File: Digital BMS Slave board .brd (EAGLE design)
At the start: 54.6 x 100 mm, 91 parts, among them J1 S7B-PH-K

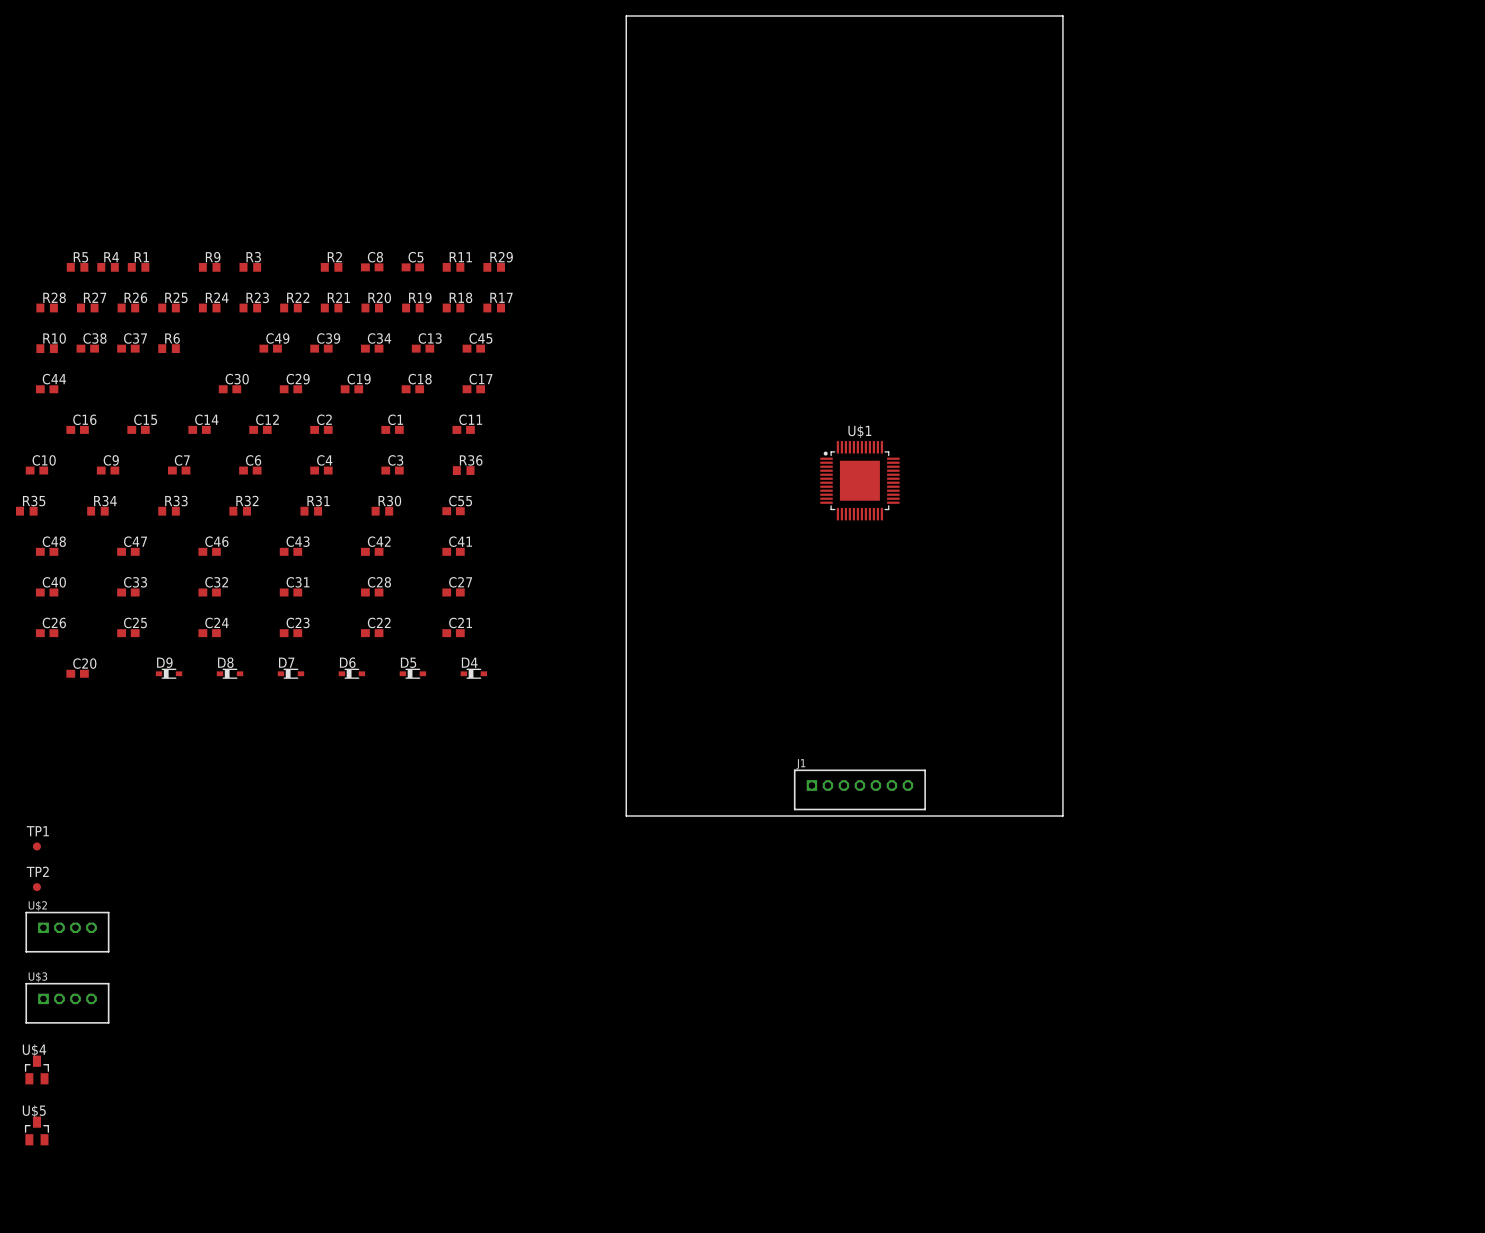
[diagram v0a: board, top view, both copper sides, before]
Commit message: Board size to chek
The schematic file is close to release ver.
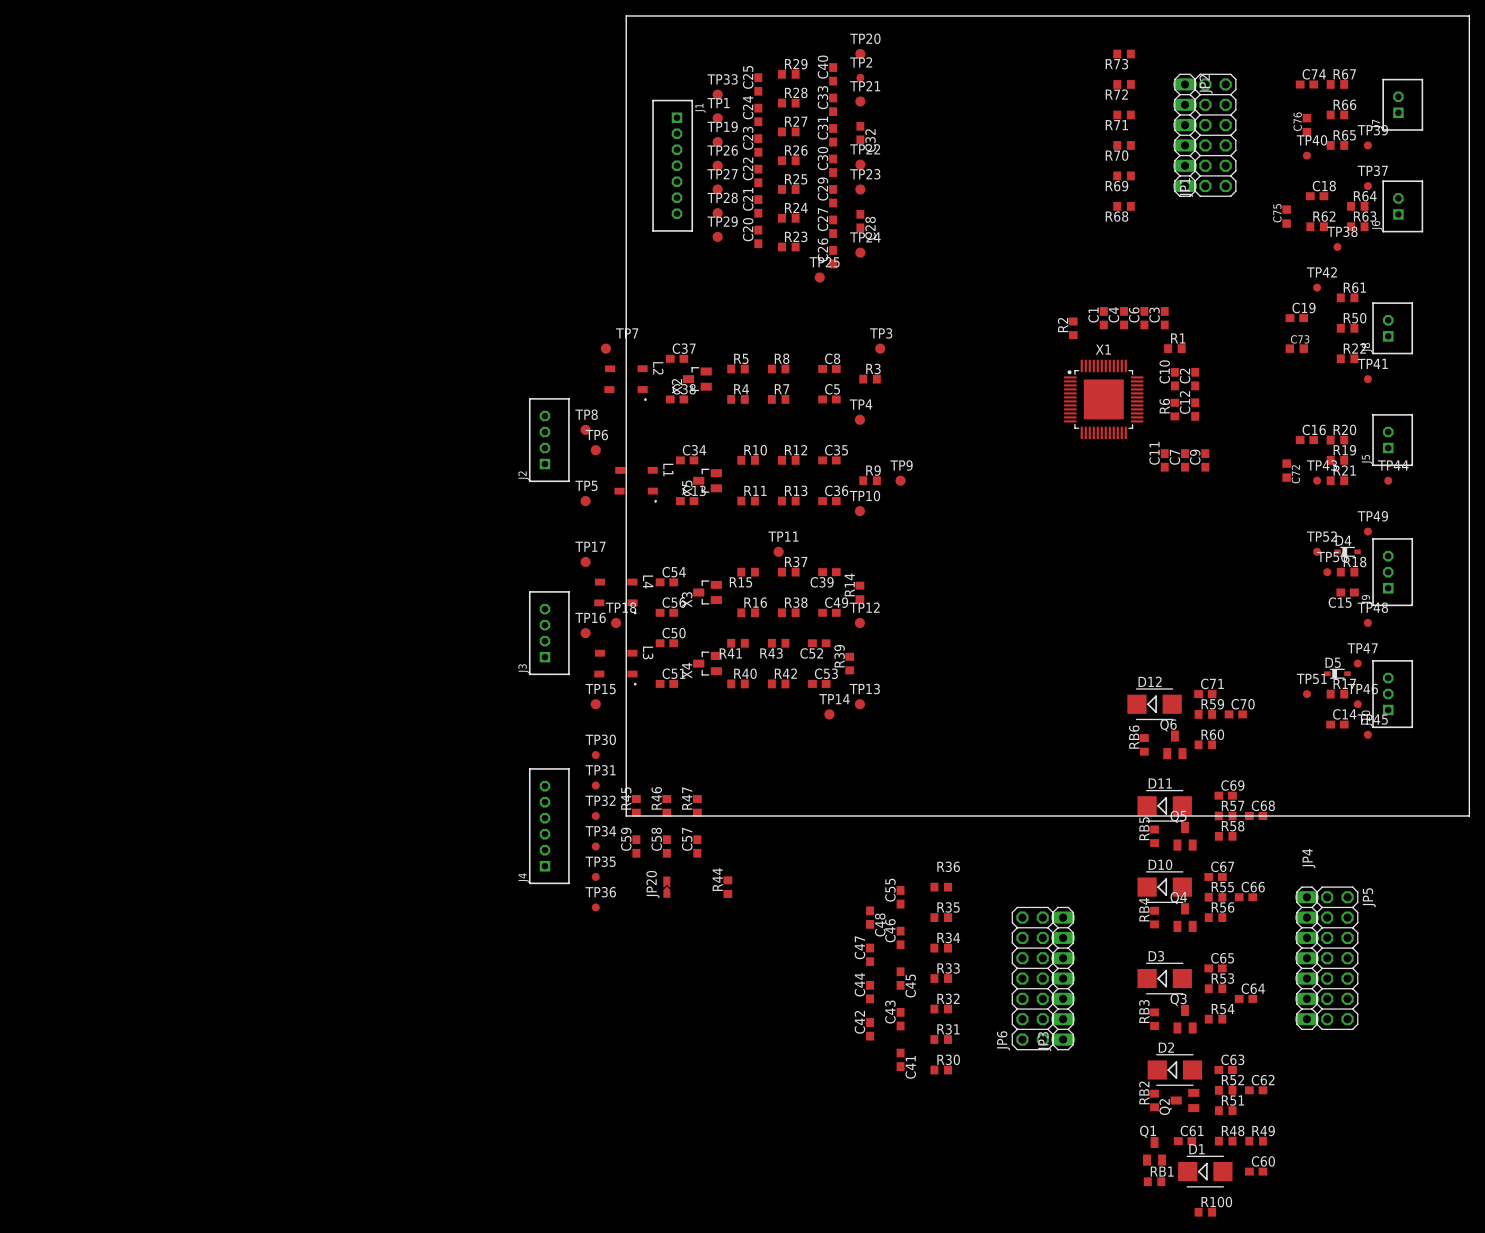
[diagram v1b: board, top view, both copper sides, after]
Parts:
- removed C17: 1u/16V, resistor:C0603
- removed D6, D7, D8, D9: BAT60J, diode:SOD323_ST
- removed U$1: BQ79606A-Q1-HTQFP(PHP)|48, texas Instrumets:QFP50P900X900X105-49T500
- removed U$2, U$3: S4B-PH-K, con-jst-ph:S4B-PH-K
- removed U$4, U$5: PESD2CAN, stmicroelectronics:SOT23
- added C35, C36, C52, C53, C57: 51p, resistor:C0603
- added C50, C51, C54, C56: 2200p, resistor:C0603
- added C58, C59: 1nF, resistor:C0603
- added C60, C61, C62, C63, C64, C65, C66, C67, C68, C69, C70, C71, C74: 1u/16V, resistor:C0603
- added C72, C73, C75, C76: 1u/16V, Capacitors:C0603K-X
- added D1, D10, D11, D12, D2, D3: (no value), eagle-ltspice:DIODE_SMB
- added J10, J9: S3B-PH-K, con-jst-ph:S3B-PH-K
- added J2, J3: S4B-PH-K, con-jst-ph:S4B-PH-K
- added J4: S6B-PH-K, con-jst-ph:S6B-PH-K
- added J5, J6, J7, J8: S2B-PH-K, con-jst-ph:S2B-PH-K
- added JP1: (no value), pinhead:2X06
- added JP2: (no value), pinhead:1X06
- added JP20: SOLDER_BRIDGE, testing:SOLDER_BRIDGE
- added JP3, JP4: (no value), pinhead:1X07
- added JP5, JP6: (no value), pinhead:2X07
- added L1, L2, L3, L4: 100uH, Inductors:ACT45B
- added Q1, Q2, Q3, Q4, Q5, Q6: BSS123, transistor-small-signal:SOT23
- added R100, R49, R52, R54, R56, R58, R60: 100, resistor:R0603
- added R12, R13, R37, R38, R42, R43, R7, R8: 43, resistor:R0603
- added R14, R39: 10k, resistor:R0603
- added R15, R16, R40, R41: 10, resistor:R0603
- added R44, R45, R46, R47: 100k, resistor:R0603
- added R48, R51, R53, R55, R57, R59, R62, R65: 1k, resistor:R0603
- added R50, R61, R63, R64, R66, R67: (no value), Resistors:R0603
- added R68, R69, R70, R71, R72, R73: 10k, Resistors:R0603
- added RB1, RB2, RB3, RB4, RB5, RB6: 20, resistor:R0603
- added TP10, TP11, TP12, TP13, TP14, TP15, TP16, TP17, TP18, TP19, TP20, TP21, TP22, TP23, TP24, TP25, TP26, TP27, TP28, TP29, TP3, TP33, TP4, TP5, TP6, TP7, TP8, TP9: TEST_PAD2, testing:TP1.27MM_MASK
- added TP30, TP31, TP32, TP34, TP35, TP36, TP37, TP38, TP39, TP40, TP41, TP42, TP43, TP44, TP45, TP46, TP47, TP48, TP49, TP50, TP51, TP52: TEST_PAD, testing:TP1MM_MASK
- added X1: BQ79606A-Q1-HTQFP(PHP)|48, texas Instrumets:QFP50P900X900X105-49T500
- added X2, X3, X4, X5: PESD2CAN, stmicroelectronics:SOT23
- C37, C38: value 51p -> 2200p
- C39, C49: value 2200p -> 51p
- D4, D5: value BAT60J -> 6.5V
- R10, R11, R4, R5: value 49 -> 10
- R20, R21: value 1k -> (none); device resistor:R0603 -> Resistors:R0603
- TP1: value TEST_PAD -> TEST_PAD2; device testing:TP1MM_MASK -> testing:TP1.27MM_MASK
- moved C16 153.7 mm to (85.1, 47.0)
- moved C15 152.5 mm to (90.2, 27.9), turned to 180 degrees
- moved C14 146.9 mm to (88.9, 11.4)
- moved TP2 144.3 mm to (29.3, 92.3)
- moved C10 142.7 mm to (68.6, 54.6), turned to 90 degrees
- moved C9 137.2 mm to (72.4, 44.5), turned to 90 degrees
- moved R22 132.2 mm to (90.2, 57.1)
- moved R1 129.9 mm to (68.6, 58.4)
- moved R21 127.6 mm to (88.9, 41.9)
- moved C44 127.5 mm to (30.5, -22.0), turned to 90 degrees
- moved R6 126.0 mm to (68.6, 50.8), turned to 90 degrees
- moved C7 125.7 mm to (69.8, 44.5), turned to 90 degrees
- moved R35 125.1 mm to (39.4, -12.7)
- moved TP1 124.6 mm to (11.4, 87.2)
- moved R20 121.8 mm to (88.9, 47.0)
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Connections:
- removed net N$28: C46.1, C47.1, C48.2, R35.2, U$1.11
- new net 123: JP6.12, R35.1
- new net 1234: JP6.14, R36.1
- new net AVDD: C6.1, X1.44
- new net BAT1: C24.1, C25.2, J1.2, JP6.11, R28.1, TP1.1
- new net BAT105: JP6.6, R32.1
- new net BAT2: C23.1, C24.2, J1.3, JP6.9, R27.1, TP19.1
- new net BAT3: C22.1, C23.2, J1.4, JP6.7, R26.1, TP26.1
- new net BAT4: C21.1, C22.2, J1.5, JP6.5, R25.1, TP27.1
- new net BAT5: C20.1, C21.2, J1.6, JP6.3, R24.1, TP28.1
- new net BAT59: JP6.4, R31.1
- new net BAT65: JP6.8, R33.1
- new net BAT75: JP6.10, R34.1
- new net CB0: JP5.13, X1.13
- new net CB1: JP5.11, X1.11
- new net CB2: JP5.9, X1.9
- new net CB3: JP5.7, X1.7
- new net CB4: JP5.5, X1.5
- new net CB5: JP5.3, X1.3
- new net CB6: JP5.1, X1.1
- new net COMHN: C53.2, R39.1, R43.1, TP14.1, X1.21
- new net COMHP: C52.2, R39.2, R42.1, TP13.1, X1.22
- new net FAULTHN: C49.2, R14.1, R38.1, TP12.1, X1.23
- new net FAULTHP: C39.2, R14.2, R37.1, TP11.1, X1.24
- new net FAULTLN: C8.2, R3.1, R8.1, TP4.1, X1.18
- new net FAULTLP: C5.2, R3.2, R7.1, TP3.1, X1.17
- new net GPIO1: JP1.2, X1.27
- new net GPIO1V2: C14.2, D5.C, JP1.1, R17.1, TP51.1
- new net GPIO2: JP1.4, X1.28
- new net GPIO2V1: C15.2, D4.C, JP1.3, R18.1, TP52.1
- new net GPIO3: JP1.6, X1.29
- new net GPIO3T4: C74.2, JP1.5, R65.1, TP40.1
- new net GPIO4: JP1.12, X1.30
- new net GPIO4T3: C18.2, JP1.7, R62.1, TP38.1
- new net GPIO5: JP1.10, X1.31
- new net GPIO5T2: C19.2, JP1.9, R22.1, TP42.1
- new net GPIO6: JP1.8, X1.32
- new net GPIO6T1: C16.2, JP1.11, R19.1, TP43.1
- new net ISO_COMHN: J3.4, L4.3, TP17.1
- new net ISO_COMHP: J3.3, L4.4, TP18.1
- new net ISO_COMLN: J2.4, L2.3, TP7.1
- new net ISO_COMLP: J2.3, L2.4, TP8.1
- new net ISO_FAULTHN: J3.2, L3.3, TP16.1
- new net ISO_FAULTHP: J3.1, L3.4, TP15.1
- new net ISO_FAULTN: J2.2, L1.3, TP6.1
- new net ISO_FAULTP: J2.1, L1.4, TP5.1
- new net N$41: R5.1, R8.2, X2.2
- new net N$42: R4.1, R7.2, X2.1
- new net N$43: R11.1, R13.2, X5.2
- new net N$44: R10.1, R12.2, X5.1
- new net N$45: C38.1, L2.1
- new net N$46: C37.1, L2.2
- new net N$47: C50.2, R16.2
- new net N$48: C51.2, R15.2
- new net N$53: C54.2, R41.2
- new net N$54: C56.2, R40.2
- new net N$55: R41.1, R43.2, X4.2
- new net N$56: R40.1, R42.2, X4.1
- new net N$57: C56.1, L4.1
- new net N$58: C54.1, L4.2
- new net N$60: C63.2, D2.C, Q2.1, R51.1
- new net N$61: C62.1, C64.2, JP4.3, R51.2, R52.2
- new net N$62: C65.2, D3.C, Q3.1, R53.1
- new net N$63: Q4.3, RB4.1
- new net N$64: C65.1, D3.A, JP3.4, Q3.2, R54.1, RB4.2
- new net N$65: C64.1, C66.2, JP4.4, R53.2, R54.2
- new net N$66: C66.1, C68.2, JP4.5, R55.2, R56.2
- new net N$67: C67.1, D10.A, JP3.5, Q4.2, R56.1, RB5.2
- new net N$68: C67.2, D10.C, Q4.1, R55.1
- new net N$69: C44.1, C45.2, JP5.8, R33.2
- new net N$70: C69.2, D11.C, Q5.1, R57.1
- new net N$71: Q6.3, RB6.1
- new net N$72: C69.1, D11.A, JP3.6, Q5.2, R58.1, RB6.2
- new net N$73: C68.1, C70.2, JP4.6, R57.2, R58.2
- new net N$74: C70.1, JP4.7, R59.2, R60.2
- new net N$75: C71.1, D12.A, JP3.7, Q6.2, R60.1
- new net N$76: C71.2, D12.C, Q6.1, R59.1
- new net N$77: C48.1, C55.2, JP5.14, R36.2
- new net N$78: C41.2, JP5.2, R30.2
- new net N$79: C46.1, C47.1, C48.2, JP5.12, R35.2
- new net N$80: C45.1, C46.2, C47.2, JP5.10, R34.2
- new net N$81: C42.1, C43.1, C44.2, JP5.6, R32.2
- new net N$83: C31.1, C32.1, C33.2, R28.2, TP2.1, X1.12
- new net NFAULT: C59.2, J4.5, R45.1, TP35.1, X1.42
- new net REF1: C4.1, X1.46
- new net RX: C57.2, J4.3, R47.1, TP32.1, X1.41
- new net TSREF: C3.1, C72.1, C73.1, C75.1, C76.1, J10.1, J9.1, R20.2, R50.2, R63.2, R66.2, TP45.1, TP48.1, X1.43
- new net TX: J4.2, TP31.1, X1.40
- new net VCC15: JP6.2, R30.1
- new net VIO: C11.1, C7.1, C9.1, J4.1, R45.2, R46.2, R47.2, TP30.1, X1.25, X1.33, X1.39
- new net WAKEUP: C58.2, J4.4, JP20.2, R46.1, TP34.1, X1.16
- net COMLN: now also C36.2, R13.1, TP10.1, X1.20; no longer C38.1, R11.1, U$1.20
- net COMLP: now also C35.2, R12.1, TP9.1, X1.19; no longer C37.2, R10.1, U$1.19
- net GND: now also C25.1, C35.1, C36.1, C39.1, C49.1, C52.1, C53.1, C57.1, C58.1, C59.1, C72.2, C73.2, C74.1, C75.2, C76.2, C8.1, J10.3, J4.6, J5.2, J6.2, J7.2, J8.2, J9.3, JP20.1, JP6.13, R21.1, R29.1, R61.1, R64.1, R67.1, R68.2, R69.2, R70.2, R71.2, R72.2, R73.2, TP33.1, TP36.1, TP47.1, TP50.1, X1.15, X1.26, X1.35, X1.45, X2.3, X3.3, X4.3, X5.3; no longer C17.1, C37.1, C38.2, C8.2, D6.A, D7.A, D8.A, D9.A, U$1.15, U$1.26, U$1.35, U$1.45
- net N$1: now also X1.48; no longer U$1.48
- net N$10: now also J6.1, R62.2, R63.1, R64.2, TP37.1; no longer C22.1, C23.2, J1.4, R26.1, R33.1
- net N$11: now also J7.1, R65.2, R66.1, R67.2, TP39.1; no longer C23.1, C24.2, J1.3, R27.1, R34.1
- net N$12: now also JP2.1, R73.1; no longer C24.1, C25.2, J1.2, R28.1, R35.1, TP1.1
- net N$13: now also TP24.1, X1.4; no longer U$1.4
- net N$14: now also C41.1, C42.2, C43.2, JP5.4, R31.2; no longer C27.1, C28.1, C29.2, R25.2, U$1.6
- net N$15: now also TP22.1, X1.8; no longer U$1.8
- net N$16: now also TP21.1, X1.10; no longer U$1.10
- net N$17: now also C27.1, C28.1, C29.2, R25.2, TP23.1, X1.6; no longer C31.1, C32.1, C33.2, R28.2, TP2.1, U$1.12
- net N$18: now also TP20.1, X1.14; no longer U$1.14
- net N$19: now also JP2.2, R72.1; no longer C42.1, C43.1, C44.2, R32.2, U$1.5
- net N$2: now also X1.37; no longer U$1.37
- net N$20: now also JP2.3, R71.1; no longer C44.1, C45.2, R33.2, U$1.7
- net N$21: now also JP2.4, R70.1; no longer C45.1, C46.2, C47.2, R34.2, U$1.9
- net N$22: now also Q3.3, RB3.1; no longer C3.1, U$1.43
- net N$23: now also JP2.5, R69.1; no longer C48.1, C55.2, R36.2, U$1.13
- net N$24: now also JP2.6, R68.1; no longer C41.1, C42.2, C43.2, R31.2, U$1.3
- net N$25: now also J10.2, R17.2, TP46.1; no longer C25.1, R29.1, R36.1
- net N$26: now also TP25.1, X1.2; no longer U$1.2
- net N$27: now also J9.2, R18.2, TP49.1; no longer C20.1, C21.2, J1.6, R24.1, R31.1
- net N$29: now also C63.1, D2.A, JP3.3, Q2.2, R52.1, RB3.2; no longer C14.2, D9.C, R17.1, U$1.27
- net N$3: now also Q1.3, RB1.1; no longer C11.1, C7.1, C9.1, U$1.25, U$1.33, U$1.39
- net N$30: now also C61.2, D1.C, Q1.1, R48.1; no longer C19.2, D4.C, R22.1, U$1.32
- net N$31: now also Q2.3, RB2.1; no longer C18.2, D5.C, R21.1, U$1.31
- net N$32: now also C61.1, D1.A, JP3.2, Q1.2, R49.1, RB2.2; no longer C17.2, D6.C, R20.1, U$1.30
- net N$33: now also C60.1, C62.2, JP4.2, R48.2, R49.2; no longer C16.2, D7.C, R19.1, U$1.29
- net N$34: now also Q5.3, RB5.1; no longer C15.2, D8.C, R18.1, U$1.28
- net N$35: now also C37.2, R11.2; no longer C5.2, R3.2, R4.1, U$1.17
- net N$36: now also C38.2, R10.2; no longer C8.1, R3.1, R5.1, U$1.18
- net N$39: now also L1.1; no longer U$2.1
- net N$4: now also JP3.1, R100.1, RB1.2; no longer C6.1, U$1.44
- net N$40: now also L1.2; no longer U$2.2
- net N$49: now also R16.1, R38.2, X3.2; no longer C39.2, R11.2
- net N$5: now also X1.36; no longer U$1.36
- net N$50: now also R15.1, R37.2, X3.1; no longer C49.2, R10.2
- net N$51: now also C51.1, L3.1; no longer C49.1, U$2.3
- net N$52: now also C50.1, L3.2; no longer C39.1, U$2.4
- net N$6: now also C60.2, JP4.1, R100.2; no longer C4.1, U$1.46
- net N$7: now also X1.34; no longer U$1.34
- net N$8: now also J8.1, R22.2, R50.1, R61.2, TP41.1; no longer C41.2, R30.2, U$1.1
- net N$9: now also J5.1, R19.2, R20.1, R21.2, TP44.1; no longer C21.1, C22.2, J1.5, R25.1, R32.1
- net VCC: now also JP6.1, TP29.1; no longer R30.1
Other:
- board size 54.6 x 100 mm -> 105.4 x 100 mm

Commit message: 3d models fixed
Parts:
- removed D10, D11, D12: (no value), eagle-ltspice:DIODE_SMB
- added D6, D7, D8: 6.5V, Semiconductor_devices:SOD323_ST
- D1, D2, D3: value (none) -> 6.5V; device eagle-ltspice:DIODE_SMB -> Semiconductor_devices:SOD323_ST
- D4, D5: device diode:SOD323_ST -> Semiconductor_devices:SOD323_ST
- JP2: device pinhead:1X06 -> commonly used connectors:1X06
- JP3, JP4: device pinhead:1X07 -> commonly used connectors:1X07
- moved C64 11.5 mm to (66.0, -21.6)
- moved C70 11.4 mm to (64.8, 12.7)
- moved C66 10.5 mm to (67.3, -7.62)
- moved C62 9.25 mm to (69.8, -31.8)
- moved D3 9.25 mm to (69.8, -29.2)
- moved C68 8.98 mm to (69.8, 1.27)
- moved C65 4.58 mm to (69.8, -21.6)
- moved R49 4.58 mm to (74.9, -43.2)
- moved R100 4.02 mm to (71.1, -45.7)
- moved C60 4.02 mm to (74.9, -45.7)
- moved R59 3.81 mm to (68.6, 12.7)
- moved J1 2.84 mm to (3.81, 82.5)
- moved C71 2.54 mm to (72.4, 12.7)
- moved D2 2.54 mm to (66.0, -31.8)
- moved D1 1.80 mm to (71.1, -43.2)
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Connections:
- net N$67: now also D7.A; no longer D10.A
- net N$68: now also D7.C; no longer D10.C
- net N$70: now also D8.C; no longer D11.C
- net N$72: now also D8.A; no longer D11.A
- net N$75: now also D6.A; no longer D12.A
- net N$76: now also D6.C; no longer D12.C

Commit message: Schematic in accordance with BOM
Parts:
- added D9: GREEN, Semiconductor_devices:LED-0805
- added J11: S4B-PH-K, con-jst-ph:S4B-PH-K
- added R74: 100, resistor:R0603
- added TP53, TP54, TP55, TP56, TP57, TP58, TP59, TP60, TP61, TP62, TP63, TP64, TP65, TP66, TP67, TP68, TP69, TP70: TEST_PAD1, testing:TP1MM_NOMASK
- C1, C2: value 33u/50V -> 0.33u/50V; device resistor:C0603 -> Capacitors:C1206K
- C13, C34, C37, C38, C50, C51, C54, C56: value 2200p -> 2.2n; device resistor:C0603 -> Capacitors:C1206K
- C20, C21, C22, C23, C24, C25: device resistor:C0603 -> Capacitors:C1206K
- C29, C30, C44, C45: device resistor:C0603 -> Capacitors:C0805K
- D1, D2, D3, D4, D5, D6, D7, D8: value 6.5V -> 6.2V
- JP3, JP4: value (none) -> 1x7
- JP5, JP6: value (none) -> 2x7
- R1: value 47 -> 47, 0.25W; device resistor:R0603 -> Resistors:R1206
- R20, R50: value (none) -> 100k
- R21, R61, R64, R67: device Resistors:R0603 -> Resistors:R0603-X
- R44: value 100k -> 1k; device resistor:R0603 -> Resistors:R0603
- R45, R46, R47: value 100k -> 10k
- R6: device resistor:R0603 -> Resistors:R0603
- R63, R66: value (none) -> 10k
- moved R44 149.5 mm to (-12.7, -156.2), turned to 0 degrees
- renumbered X1 to U1
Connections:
- new net N$28: D9.+, R44.1
- new net RX1: C57.2, J4.3, R47.1, R74.1, TP32.1
- net AVDD: now also R44.2
- net GND: now also D9.-
- net GPIO3: now also J11.4
- net GPIO4: now also J11.3
- net GPIO5: now also J11.2
- net GPIO6: now also J11.1
- net N$22: now also TP59.1
- net N$3: now also TP62.1
- net N$30: now also TP53.1
- net N$31: now also TP61.1
- net N$33: now also TP66.1
- net N$34: now also TP64.1
- net N$6: now also TP65.1
- net N$60: now also TP54.1
- net N$61: now also TP67.1
- net N$62: now also TP55.1
- net N$63: now also TP60.1
- net N$65: now also TP68.1
- net N$66: now also TP69.1
- net N$68: now also TP56.1
- net N$70: now also TP57.1
- net N$71: now also TP63.1
- net N$73: now also TP70.1
- net N$76: now also TP58.1
- net RX: now also R74.2; no longer C57.2, J4.3, R47.1, TP32.1

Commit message: Footprint fixed
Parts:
- R30, R31, R32, R33, R34, R35, R36: device resistor:R0603 -> resistor:R1210
- RB1, RB2, RB3, RB4, RB5, RB6: device resistor:R0603 -> Resistors:R2512
